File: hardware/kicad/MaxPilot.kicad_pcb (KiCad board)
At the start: 2 copper layers, 99.1 x 38.1 mm, 16 parts, among them J1 Conn_01x03, U1 WeMos_D1_mini, U2 MOC3041M, U3 MOC3041M

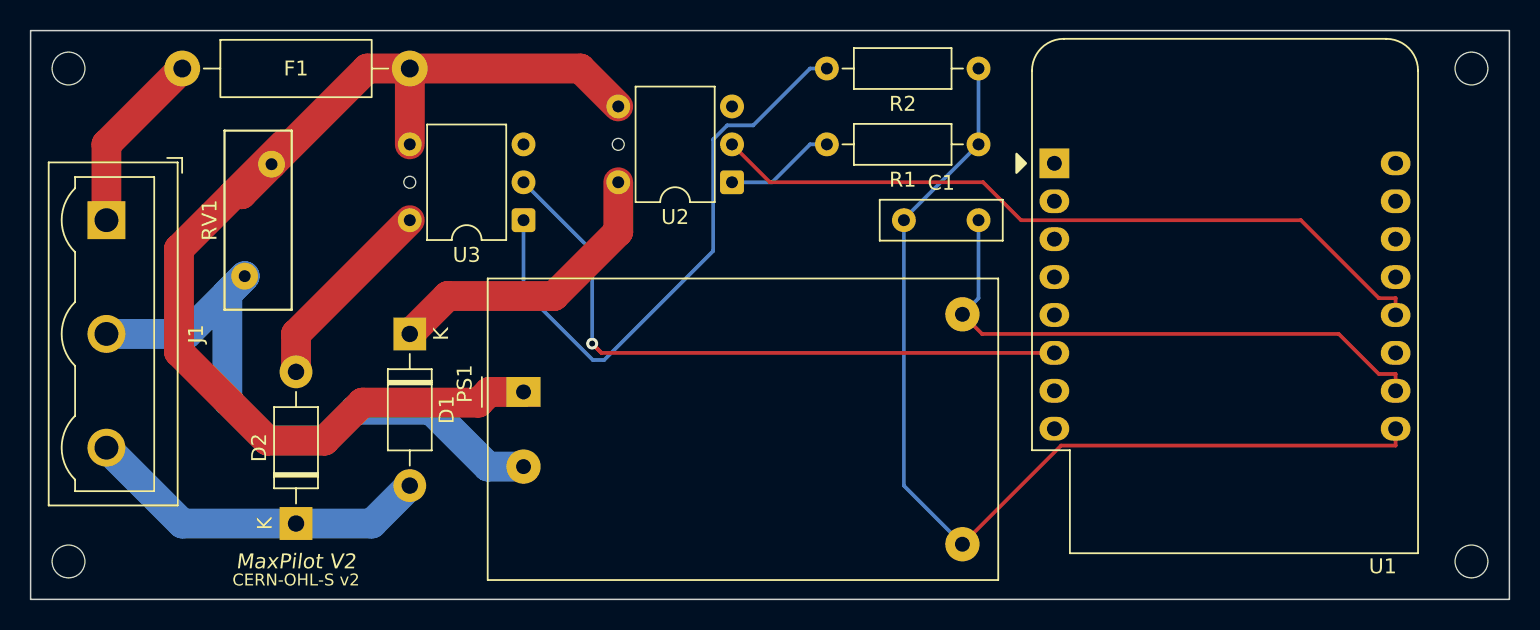
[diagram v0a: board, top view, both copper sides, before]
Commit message: Reroute PCB: mains traces moved to B.Cu, no vias
All LINE/NEUT traces now routed on back copper layer, eliminating vias
and improving mains isolation. Regenerate Gerbers and PCB images.

Co-Authored-By: Claude Sonnet 4.6 <noreply@anthropic.com>
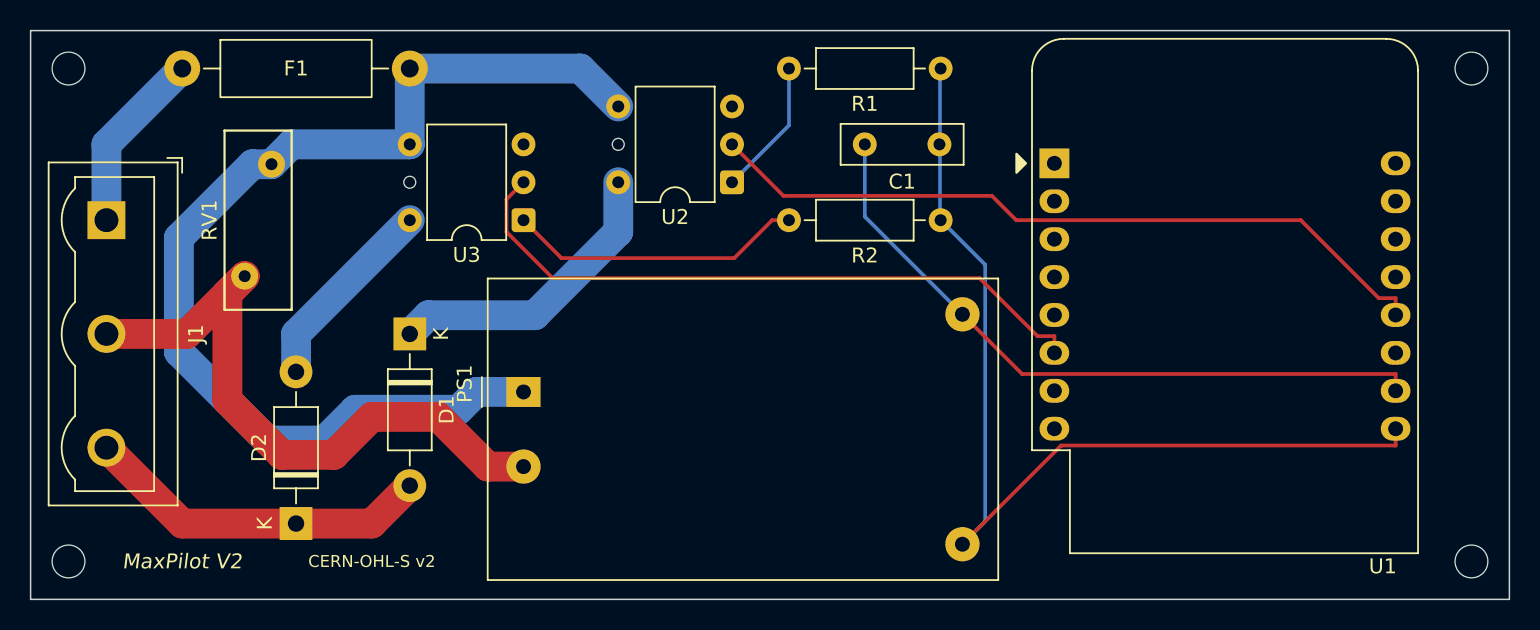
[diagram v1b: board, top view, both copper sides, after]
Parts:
- moved R2 10.5 mm to (73.7, 25.4)
- moved R1 5.68 mm to (73.7, 15.2)
- moved C1 5.61 mm to (73.6, 20.3), turned to 180 degrees
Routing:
- net Net-(R2-Pad2): track 39.4 -> 19.9 mm
- net GND: track 38.6 -> 45.9 mm
- net LINE_P: track 79.1 -> 72.7 mm
- net Net-(R1-Pad2): track 7.41 -> 9.20 mm
- net +5V: track 68.4 -> 66.7 mm
- net Net-(U1-MOSI/D7): track 45.7 -> 44.5 mm, vias 1 -> 0
